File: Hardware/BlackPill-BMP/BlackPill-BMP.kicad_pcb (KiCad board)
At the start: 2 copper layers, 72.5 x 59.7 mm, 41 parts, among them J1 JTAG, J10 Conn_01x12_Male, J2 VCC, J3 GND, J4 SWO, J5 GDB_COMM, J6 TVCC, J7 LogicAna, J8 Conn_01x06_Male, J9 Conn_01x05_Male, U1 BlueAndBlackPill, U2 AD8531ARTZ, U3 74LVC2T45DC, U4 74LS125, U5 74LS125, U6 SRV05-4, U7 SRV05-4

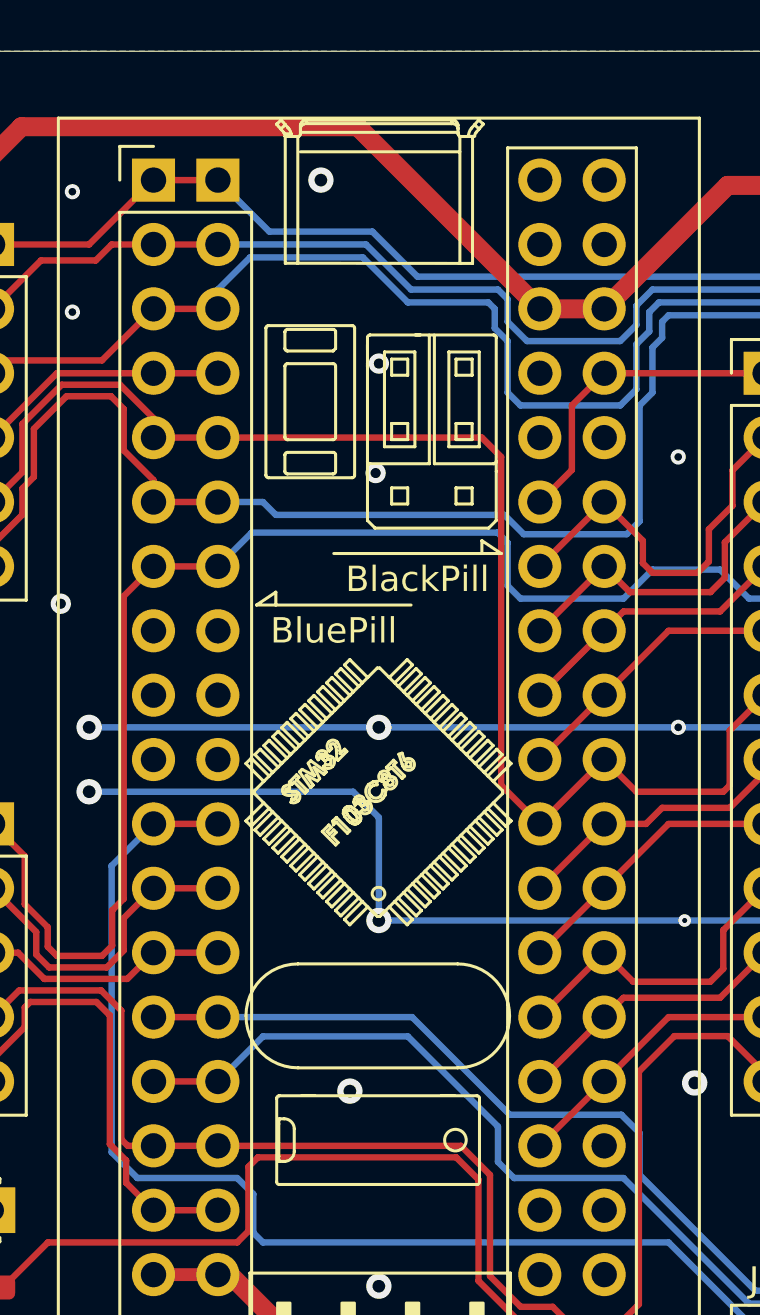
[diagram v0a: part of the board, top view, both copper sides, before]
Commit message: Updated BOM on the schematics for the BluePill/BlackPill design (no PCB or fabrication changes).
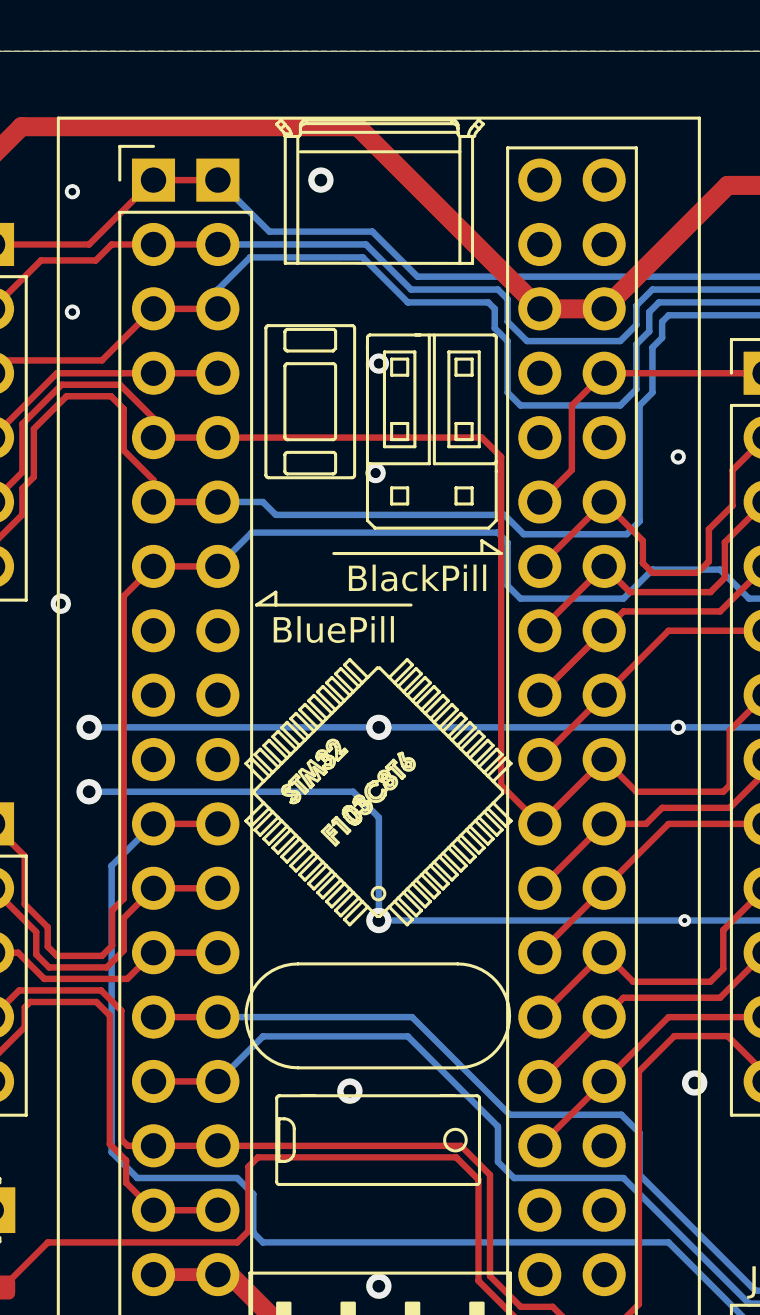
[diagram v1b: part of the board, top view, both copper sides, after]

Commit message: BluePill/BlackPill Prototype: Fixed LED part number
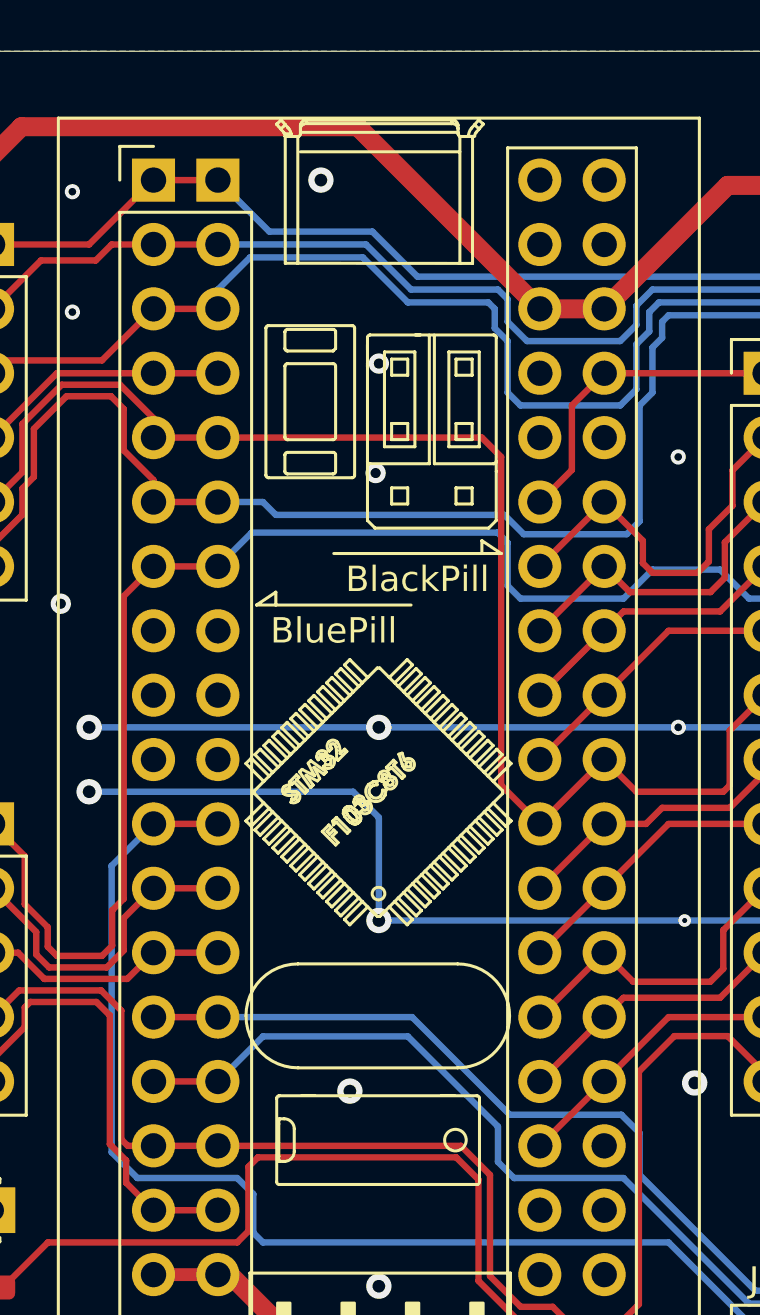
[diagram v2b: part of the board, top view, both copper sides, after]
